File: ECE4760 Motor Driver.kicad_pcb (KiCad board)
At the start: 6 copper layers, 43.2 x 52.1 mm, 156 parts, among them J1 IO, J100 Alternative Motor, J2 Motor / Power, J4 UART, J5 Debug, Q1 EPC23104, Q2 EPC23104, Q3 EPC23104, Q4 EPC23104, SW1 BOOT, U1 STM32G473V_B-C-E_Hx, U2 ACS711xEXLT-15AB, U3 ACS711xEXLT-15AB, U4 ACS711xEXLT-15AB, U5 AP7361C-33FGE, U6 ACS711xEXLT-15AB, U7 TPSM365R6, X1 48MHz

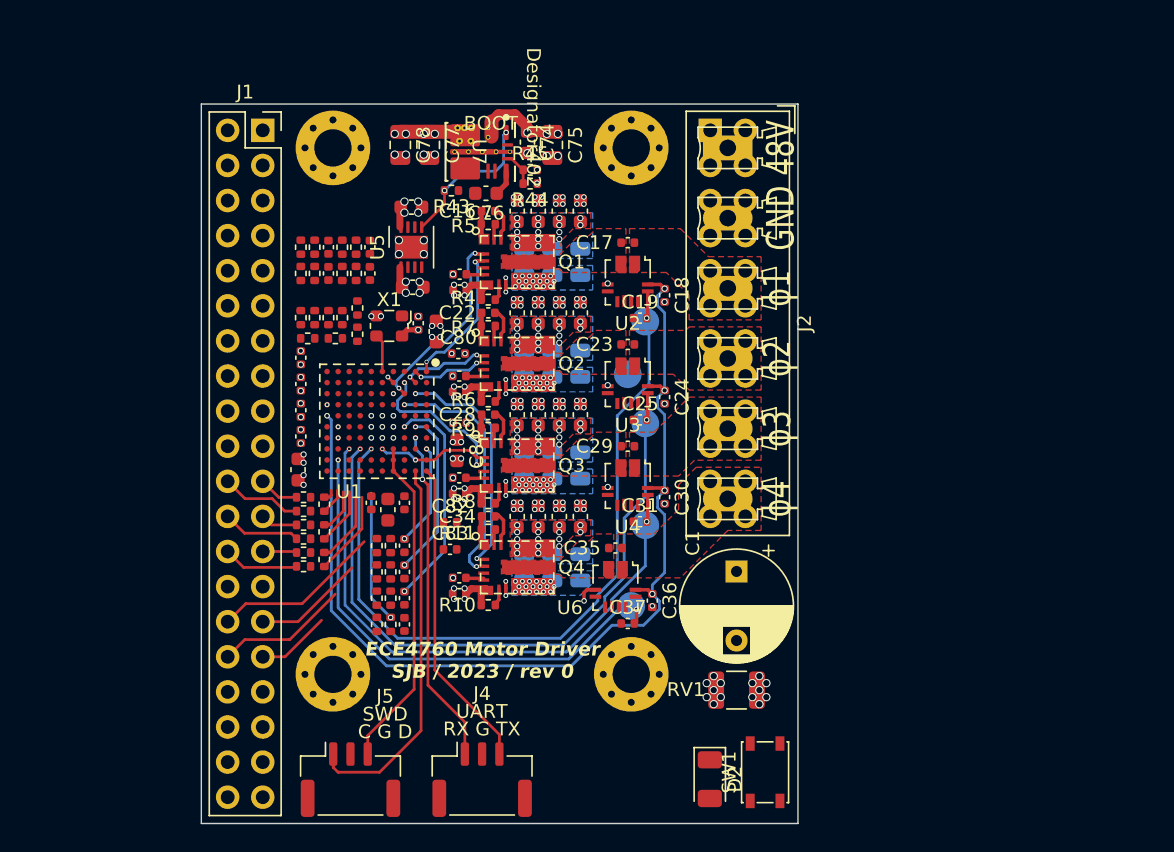
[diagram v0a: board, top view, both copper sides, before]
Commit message: Limit switch inputs and silkscreen
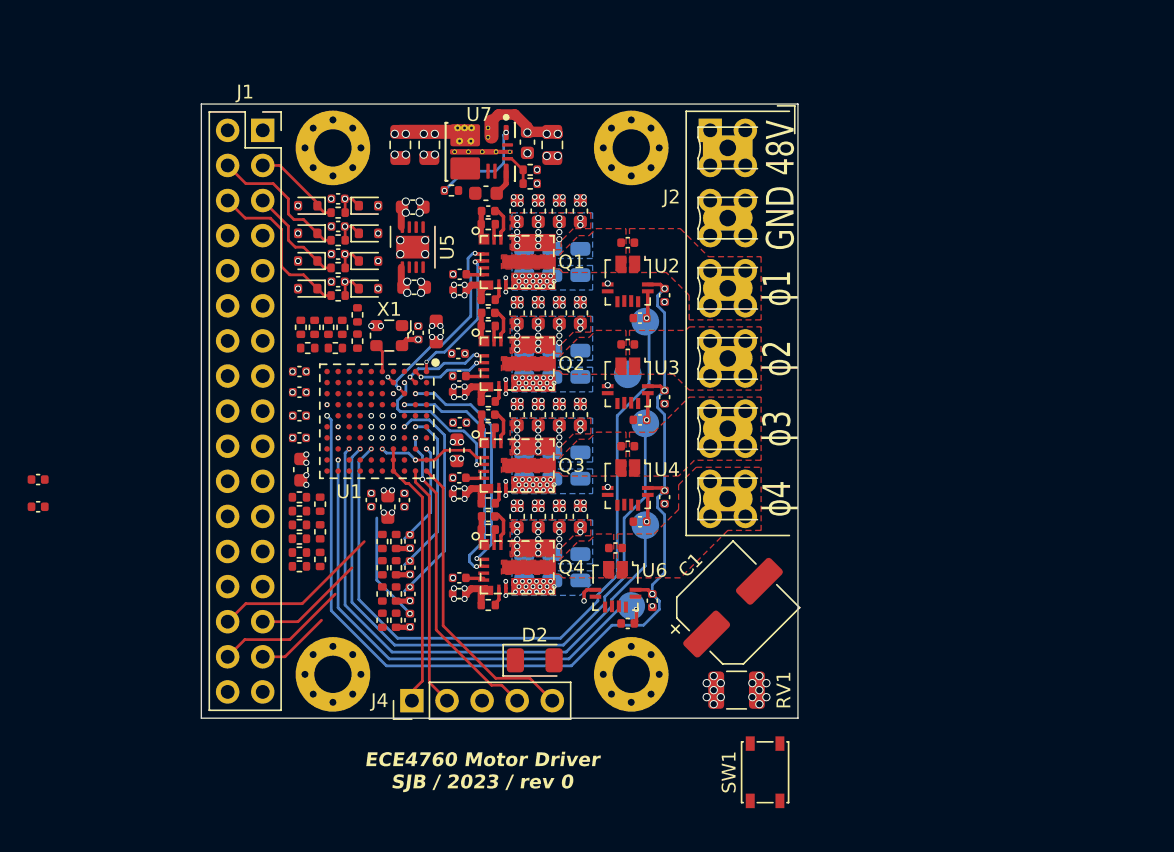
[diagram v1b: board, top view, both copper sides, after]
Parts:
- removed J5: Debug, Connector_JST:JST_GH_SM03B-GHS-TB_1x03-1MP_P1.25mm_Horizontal
- removed R36, R38, R40, R42: 1k, Resistor_SMD:R_0402_1005Metric
- added D1: D_Zener, Diode_SMD:D_SOD-523, F.Cu at (88.3, 50.0)
- added D3: D_Zener, Diode_SMD:D_SOD-523, F.Cu at (88.3, 48.0)
- added D4: D_Zener, Diode_SMD:D_SOD-523, F.Cu at (88.3, 54.0)
- added D5: D_Zener, Diode_SMD:D_SOD-523, F.Cu at (88.3, 52.0)
- added D6: D_Schottky, Diode_SMD:D_SOD-523, F.Cu at (83.9, 50.0)
- added D7: D_Schottky, Diode_SMD:D_SOD-523, F.Cu at (83.9, 48.0)
- added D8: D_Schottky, Diode_SMD:D_SOD-523, F.Cu at (83.9, 54.0)
- added D9: D_Schottky, Diode_SMD:D_SOD-523, F.Cu at (83.9, 52.0)
- C1: footprint Capacitor_THT:CP_Radial_D8.0mm_P5.00mm -> Capacitor_SMD:CP_Elec_6.3x7.7
- J1: footprint Connector_PinSocket_2.54mm:PinSocket_2x20_P2.54mm_Vertical -> Connector_PinSocket_2.54mm:PinSocket_2x17_P2.54mm_Vertical
- J4: footprint Connector_JST:JST_GH_SM03B-GHS-TB_1x03-1MP_P1.25mm_Horizontal -> Connector_PinHeader_2.54mm:PinHeader_1x05_P2.54mm_Vertical
- moved C82 30.0 mm to (64.4, 67.8)
- moved C83 30.0 mm to (64.4, 69.8)
- moved D2 15.3 mm to (100.3, 80.9), turned to 0 degrees
- moved J4 7.65 mm to (91.4, 83.8), turned to 90 degrees
- moved C71 5.45 mm to (86.1, 47.5), turned to 180 degrees
- moved R37 5.16 mm to (86.1, 48.5), turned to 0 degrees
- moved R39 3.51 mm to (86.1, 54.5), turned to 0 degrees
- moved C72 3.40 mm to (86.1, 53.5), turned to 180 degrees
- moved R35 2.75 mm to (86.1, 50.5), turned to 0 degrees
- moved C73 2.69 mm to (86.1, 51.5), turned to 180 degrees
- moved C1 2.63 mm to (114.7, 77.1), turned to 45 degrees
- moved C70 1.66 mm to (86.1, 49.5), turned to 180 degrees
- moved C9 1.00 mm to (83.3, 60.0), turned to 180 degrees
- moved C11 0.70 mm to (91.9, 57.2)
- moved R29 0.70 mm to (83.4, 56.8)
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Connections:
- J1 pad 3: Lim_H_In -> Lim_R_In
- J1 pad 6: Lim_R_In -> Lim_H_In
- J4 pad 1: /UART_RX -> /SWDIO
- J4 pad 2: GND -> /SWCLK
- J4 pad 3: /UART_TX -> GND
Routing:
- net Lim_H_In: track 0.00 -> 11.9 mm
- net Lim_L_In: track 0.00 -> 10.4 mm
- net /SWCLK: track 27.7 -> 17.6 mm
- net Lim_Aux_In: track 0.65 -> 7.56 mm
- net Lim_R_In: track 0.00 -> 6.48 mm
- net /ENC_I+: track 6.14 -> 0.00 mm
- net Enc_A_In+: track 5.88 -> 0.00 mm
- net Enc_B_In+: track 5.65 -> 0.00 mm
- net Enc_I_In+: track 5.49 -> 0.00 mm
- net /SWDIO: track 24.1 -> 18.6 mm
- net /ENC_I-: track 5.16 -> 0.00 mm
- net /ENC_B+: track 4.17 -> 0.00 mm
- net GND: track 6.20 -> 10.2 mm, vias 209 -> 229
- net Net-(U5-EN): track 10.7 -> 7.39 mm
- net /ENC_B-: track 3.19 -> 0.00 mm
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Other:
- board size 43.2 x 52.1 mm -> 43.2 x 44.5 mm
- board text added: "Clk"
- board text added: "Data"
- board text added: "Gnd"
- board text added: "Rx"
- board text added: "Tx"
- board text removed: "5V"
- board text removed: "C G D"
- board text removed: "RX G TX"
- board text removed: "SWD"
- board text removed: "UART"

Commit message: Update hall sensor circuit for 5V-tolerant pins
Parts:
- removed R13, R15, R17, R19: 1k, Resistor_SMD:R_0402_1005Metric
- removed SW1: BOOT, Button_Switch_SMD:SW_SPST_PTS810
- added R1: 1k, Resistor_SMD:R_0402_1005Metric, F.Cu at (83.3, 63.1)
- added R36: 1k, Resistor_SMD:R_0402_1005Metric, F.Cu at (83.3, 64.1)
- added R38: 330, Resistor_SMD:R_0402_1005Metric, F.Cu at (95.9, 78.4)
- added TP6: RESET, TestPoint:TestPoint_Pad_D2.0mm, B.Cu at (84.9, 57.5)
- added TP7: BOOT, TestPoint:TestPoint_Pad_D2.0mm, B.Cu at (95.2, 56.2)
- moved C69 3.16 mm to (90.7, 74.9), turned to 0 degrees
- moved R18 3.14 mm to (88.8, 74.9), turned to 0 degrees
- moved R29 3.10 mm to (86.5, 56.8)
- moved C66 2.28 mm to (90.7, 73.9), turned to 0 degrees
- moved R12 2.26 mm to (88.8, 73.9), turned to 0 degrees
- moved R31 2.10 mm to (86.0, 58.3), turned to 0 degrees
- moved R32 1.90 mm to (83.5, 56.8)
- moved R33 1.90 mm to (84.5, 56.8)
- moved R34 1.90 mm to (84.0, 58.3)
- moved R2 1.90 mm to (87.5, 57.8), turned to 90 degrees
- moved R3 1.90 mm to (87.5, 55.9), turned to 90 degrees
- moved C68 1.43 mm to (90.7, 72.9), turned to 0 degrees
- moved R16 1.39 mm to (88.8, 72.9), turned to 0 degrees
- moved C10 1.10 mm to (83.3, 62.1)
- moved R30 1.10 mm to (85.5, 56.8)
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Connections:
- C70 pad 1: /Limit Switch Input1/Out -> /LIM_L
- C71 pad 1: /Limit Switch Input2/Out -> /LIM_R
- C72 pad 1: /Limit Switch Input3/Out -> /LIM_H
- C73 pad 1: /Limit Switch Input4/Out -> /LIM_AUX
- D1 pad 1: /Limit Switch Input1/Out -> /LIM_L
- D2 pad 1: unconnected-(D2-K-Pad1) -> GND
- D2 pad 2: unconnected-(D2-A-Pad2) -> Net-(D2-A)
- D3 pad 1: /Limit Switch Input2/Out -> /LIM_R
- D4 pad 1: /Limit Switch Input3/Out -> /LIM_H
- D5 pad 1: /Limit Switch Input4/Out -> /LIM_AUX
- J1 pad 11: Aux_Enc_A_In+ -> Aux_Enc_A_In-
- J1 pad 12: Aux_Enc_A_In- -> Aux_Enc_A_In+
- J1 pad 15: ~{Fault_Enable} -> LED_1
- J1 pad 16: ~{Abort} -> LED_2
- J1 pad 17: LED_2 -> ~{Fault_Enable}
- J1 pad 18: LED_1 -> ~{Abort}
- R2 pad 2: Net-(U1-PA1) -> Net-(R2-Pad2)
- R29 pad 1: Aux_Enc_A_In+ -> Aux_Enc_B_In+
- R29 pad 2: /AUX_ENC_A+ -> /AUX_ENC_B+
- R3 pad 1: Net-(U1-PA1) -> Net-(R2-Pad2)
- R30 pad 1: Aux_Enc_A_In- -> Aux_Enc_B_In-
- R30 pad 2: /AUX_ENC_A- -> /AUX_ENC_B-
- R31 pad 1: /AUX_ENC_A- -> /AUX_ENC_B-
- R31 pad 2: /AUX_ENC_A+ -> /AUX_ENC_B+
- R32 pad 1: Aux_Enc_B_In+ -> Aux_Enc_A_In+
- R32 pad 2: /AUX_ENC_B+ -> /AUX_ENC_A+
- R33 pad 1: Aux_Enc_B_In- -> Aux_Enc_A_In-
- R33 pad 2: /AUX_ENC_B- -> /AUX_ENC_A-
- R34 pad 1: /AUX_ENC_B- -> /AUX_ENC_A-
- R34 pad 2: /AUX_ENC_B+ -> /AUX_ENC_A+
- R35 pad 2: /Limit Switch Input1/Out -> /LIM_L
- R37 pad 2: /Limit Switch Input2/Out -> /LIM_R
- R39 pad 2: /Limit Switch Input3/Out -> /LIM_H
- R41 pad 2: /Limit Switch Input4/Out -> /LIM_AUX
- U1 pad D1: unconnected-(U1-PC15-PadD1) -> /LIM_R
- U1 pad E10: unconnected-(U1-PA8-PadE10) -> Net-(U1-PA8)
- U1 pad E2: unconnected-(U1-PF1-PadE2) -> /LIM_L
- U1 pad F1: unconnected-(U1-PC2-PadF1) -> /LIM_H
- U1 pad F10: unconnected-(U1-PC7-PadF10) -> /HALL_I
- U1 pad F2: unconnected-(U1-PC0-PadF2) -> /LIM_AUX
- U1 pad G1: /HALL_I -> /AUX_ENC_B+
- U1 pad G2: Net-(U1-PA1) -> /AUX_ENC_B+
- U1 pad G6: /AUX_ENC_A+ -> unconnected-(U1-PE12-PadG6)
- U1 pad H1: /AUX_ENC_B -> /AUX_ENC_B-
- U1 pad H2: /AUX_ENC_A+ -> /AUX_ENC_B-
- U1 pad H3: unconnected-(U1-PA3-PadH3) -> Net-(R2-Pad2)
- U1 pad H4: /AUX_ENC_A+ -> unconnected-(U1-PB0-PadH4)
- U1 pad J1: /AUX_ENC_B- -> /AUX_ENC_A-
- U1 pad J2: /AUX_ENC_A- -> unconnected-(U1-PA6-PadJ2)
- U1 pad J4: /AUX_ENC_A- -> unconnected-(U1-PB2-PadJ4)
- U1 pad J6: ~{Abort} -> unconnected-(U1-PE11-PadJ6)
- U1 pad J7: LED_2 -> unconnected-(U1-PE14-PadJ7)
- U1 pad K1: /AUX_ENC_B+ -> /AUX_ENC_A+
- U1 pad K10: LED_1 -> unconnected-(U1-PD8-PadK10)
- U1 pad K2: unconnected-(U1-PC4-PadK2) -> LED_1
- U1 pad K3: unconnected-(U1-PB1-PadK3) -> LED_2
- U1 pad K6: ~{Fault_Enable} -> Net-(U1-PE10)
- U1 pad K7: /AUX_ENC_B -> Net-(U1-PE13)
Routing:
- net /LIM_R: track 0.00 -> 17.1 mm, vias 0 -> 2
- net /LIM_L: track 0.00 -> 15.8 mm, vias 0 -> 2
- net Net-(U1-PA8): track 0.00 -> 15.0 mm, vias 0 -> 2
- net /LIM_AUX: track 0.00 -> 13.7 mm, vias 0 -> 2
- net /LIM_H: track 0.00 -> 10.7 mm, vias 0 -> 2
- net Aux_Enc_B_In-: track 0.00 -> 9.09 mm
- net /~{RST}: track 0.00 -> 8.75 mm, vias 0 -> 1
- net LED_2: track 0.00 -> 7.72 mm
- net Aux_Enc_B_In+: track 0.00 -> 7.34 mm
- net /BOOT_SELECT: track 0.00 -> 6.52 mm, vias 0 -> 1
- net Aux_Enc_A_In+: track 0.11 -> 5.92 mm
- net Net-(R2-Pad2): track 0.00 -> 5.44 mm, vias 0 -> 2
- net ~{Abort}: track 0.00 -> 5.19 mm, vias 1 -> 0
- net LED_1: track 0.00 -> 4.85 mm, vias 0 -> 1
- net Hall_I_In: track 5.35 -> 10.0 mm
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
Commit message: Ready for design review
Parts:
- removed the D5 at (88.3, 52.0)
- removed D6, D7, D8, D9: D_Schottky, Diode_SMD:D_SOD-523
- removed the R1 at (83.3, 63.1)
- removed the R36 at (83.3, 64.1)
- removed the R43 at (94.3, 46.9)
- added C81: 100n, Capacitor_SMD:C_0402_1005Metric, B.Cu at (88.8, 64.9)
- added C82: 100n, Capacitor_SMD:C_0402_1005Metric, B.Cu at (90.2, 64.5)
- added D2: BAT54XY, Package_TO_SOT_SMD:SOT-363_SC-70-6, F.Cu at (88.6, 73.2)
- added R12: 4k7, Resistor_SMD:R_0402_1005Metric, F.Cu at (90.5, 76.1)
- added R14: 4k7, Resistor_SMD:R_0402_1005Metric, F.Cu at (90.5, 78.0)
- added R16: 4k7, Resistor_SMD:R_0402_1005Metric, F.Cu at (90.5, 72.3)
- added R18: 4k7, Resistor_SMD:R_0402_1005Metric, F.Cu at (90.5, 74.2)
- added R20: 4k7, Resistor_SMD:R_0402_1005Metric, F.Cu at (87.6, 49.7)
- added R22: 4k7, Resistor_SMD:R_0402_1005Metric, F.Cu at (87.6, 47.8)
- added R24: 4k7, Resistor_SMD:R_0402_1005Metric, F.Cu at (87.6, 53.5)
- added R26: 4k7, Resistor_SMD:R_0402_1005Metric, F.Cu at (87.6, 51.6)
- C1: value 10u 100V -> 22u 100V
- C18: renamed from C16; value 100n, 6V -> 100n
- C20: renamed from C18; value 10n -> 1n
- C31: renamed from C22; value 100n, 6V -> 100n
- C33: renamed from C24; value 10n -> 1n
- C44: renamed from C28; value 100n, 6V -> 100n
- C46: renamed from C30; value 10n -> 1n
- C57: renamed from C34; value 100n, 6V -> 100n
- C59: renamed from C36; value 10n -> 1n
- C61: renamed from C66; value 10n -> 1n
- C62: renamed from C67; value 10n -> 1n
- C63: renamed from C68; value 10n -> 1n
- C64: renamed from C69; value 10n -> 1n
- C7: renamed from C76; value 1u -> 4u7
- C70: renamed from C5; value 1u -> 4u7
- C71: renamed from C4; value 1u -> 4u7
- C72: renamed from C85; value 1u -> 4u7
- C73: renamed from C84; value 1u -> 4u7
- C83: renamed from C82; moved to B.Cu
- C84: renamed from C83; moved to B.Cu
- D1, D3, D4: value D_Zener -> BAT54XY; footprint Diode_SMD:D_SOD-523 -> Package_TO_SOT_SMD:SOT-363_SC-70-6
- D5: renamed from D2; value LED -> Green
- R13: renamed from R12; value 1k -> 100
- R15: renamed from R14; value 1k -> 100
- R17: renamed from R16; value 1k -> 100
- R19: renamed from R18; value 1k -> 100
- R21: renamed from R35; value 1k -> 100
- R23: renamed from R37; value 1k -> 100
- R25: renamed from R39; value 1k -> 100
- R27: renamed from R41; value 1k -> 100
- R31: renamed from R20; value 1k, 0.1% -> 1k, 1%
- R32: renamed from R22; value 1k, 0.1% -> 1k, 1%
- R33: renamed from R21; value 1k, 0.1% -> 1k, 1%
- R34: renamed from R23; value 1k, 0.1% -> 1k, 1%
- R35: renamed from R25; value 1k, 0.1% -> 1k, 1%
- R36: renamed from R24; value 1k, 0.1% -> 1k, 1%
- R37: renamed from R26; value 1k, 0.1% -> 1k, 1%
- R38: renamed from R28; value 1k, 0.1% -> 1k, 1%
- R39: renamed from R27; value 1k, 0.1% -> 1k, 1%
- R40: renamed from R29; value 1k, 0.1% -> 1k, 1%
- R41: renamed from R31; value 1k, 0.1% -> 1k, 1%
- R42: renamed from R30; value 1k, 0.1% -> 1k, 1%
- R43: renamed from R32; value 1k, 0.1% -> 1k, 1%
- R44: renamed from R34; value 1k, 0.1% -> 1k, 1%
- R45: renamed from R33; value 1k, 0.1% -> 1k, 1%
- TP3: renamed from TP1; value TestPoint -> Sense
- TP4: renamed from TP2; value TestPoint -> Sense
- TP5: renamed from TP3; value TestPoint -> Sense
- TP6: renamed from TP4; value TestPoint -> Sense
- TP7: renamed from TP5; value TestPoint -> Sense
- moved D1 27.0 mm to (88.6, 77.0), turned to 90 degrees
- moved C83 25.8 mm to (89.8, 63.1), turned to 180 degrees
- moved C84 24.8 mm to (88.4, 63.5), turned to -90 degrees
- moved R15 6.63 mm to (86.2, 78.0)
- moved C62 6.15 mm to (91.5, 78.0), turned to 90 degrees
- moved R13 3.97 mm to (86.2, 76.9)
- moved R17 3.16 mm to (86.2, 74.7)
- moved D4 3.00 mm to (85.7, 52.5), turned to -90 degrees
- moved R19 2.75 mm to (86.2, 75.8)
- moved D3 2.67 mm to (85.7, 48.6), turned to -90 degrees
- moved C66 2.52 mm to (88.6, 47.8), turned to -90 degrees
- moved C65 2.51 mm to (88.6, 49.7), turned to 90 degrees
- moved R25 2.51 mm to (83.8, 53.5), turned to 90 degrees
- moved C68 2.50 mm to (88.6, 51.6), turned to -90 degrees
- moved C67 2.50 mm to (88.6, 53.5), turned to 90 degrees
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- renumbered C39 to C10, C40 to C11, C41 to C12, C54 to C13, C55 to C14, C56 to C15, C14 to C16, C15 to C17, C17 to C19, C74 to C2, C19 to C21, C42 to C22, C43 to C23, C44 to C24, C45 to C25, C57 to C26, C58 to C27, C59 to C28, C20 to C29, C75 to C3, C21 to C30, C23 to C32, C25 to C34, C46 to C35, C47 to C36, C48 to C37, C49 to C38, C60 to C39, C78 to C4, C61 to C40, C62 to C41, C26 to C42, C27 to C43, C29 to C45, C31 to C47, C50 to C48, C51 to C49, C77 to C5, C52 to C50, C53 to C51, C63 to C52, C64 to C53, C65 to C54, C32 to C55, C33 to C56, C35 to C58, C12 to C6, C37 to C60, C70 to C65, C71 to C66, C72 to C67, C73 to C68, C10 to C69, C79 to C74, C80 to C75, C81 to C76, C9 to C77, C8 to C78, C7 to C79, C13 to C8, C6 to C80, C11 to C85, C38 to C9, J100 to J101, J4 to J3, R44 to R1, R2 to R28, R3 to R29, R45 to R3, R38 to R30, TP6 to TP1, TP7 to TP2, U6 to U5, U5 to U6
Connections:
- C20 pad 2: VREF -> +3V3
- C33 pad 2: VREF -> +3V3
- C46 pad 2: VREF -> +3V3
- C59 pad 2: VREF -> +3V3
- C62 pad 1: /HALL_B -> /HALL_I
- C63 pad 1: /HALL_C -> /HALL_B
- C64 pad 1: /HALL_I -> /HALL_C
- D1 pad 1: /LIM_L -> GND
- D1 pad 2: GND -> +5V
- D3 pad 1: /LIM_R -> GND
- D3 pad 2: GND -> +5V
- D4 pad 1: /LIM_H -> GND
- D4 pad 2: GND -> +5V
- R15 pad 1: Hall_B_In -> Hall_I_In
- R15 pad 2: /HALL_B -> /HALL_I
- R17 pad 1: Hall_C_In -> Hall_B_In
- R17 pad 2: /HALL_C -> /HALL_B
- R19 pad 1: Hall_I_In -> Hall_C_In
- R19 pad 2: /HALL_I -> /HALL_C
- U1 pad B4: unconnected-(U1-PB7-PadB4) -> /PH4_LO
- U1 pad F10: /HALL_I -> /ENC_I+
- U1 pad F9: unconnected-(U1-PC6-PadF9) -> /HALL_I
- U1 pad G6: unconnected-(U1-PE12-PadG6) -> /AUX_ENC_A-
- U1 pad G9: unconnected-(U1-PD13-PadG9) -> /ENC_I+
- U1 pad J2: unconnected-(U1-PA6-PadJ2) -> Net-(U1-PA6)
- U1 pad J6: unconnected-(U1-PE11-PadJ6) -> ~{Abort}
- U1 pad K5: VREF -> +3V3
- U1 pad K6: Net-(U1-PE10) -> ~{Fault_Enable}
- U1 pad K7: Net-(U1-PE13) -> Net-(U1-PA6)
- U2 pad 10: VREF -> +3V3
- U3 pad 10: VREF -> +3V3
- U4 pad 10: VREF -> +3V3
- U5 pad 10: VREF -> +3V3
- U6 pad 5: Net-(U5-EN) -> +5V
- U7 pad 1: Net-(U5-EN) -> unconnected-(U7-PGOOD-Pad1)
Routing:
- net +3V3: track 6.81 -> 83.9 mm, vias 25 -> 30
- net VREF: track 71.7 -> 0.00 mm, vias 5 -> 0
- net GND: track 5.64 -> 18.3 mm, vias 242 -> 250
- net /ENC_I+: track 0.00 -> 11.4 mm
- net Net-(U5-EN): track 10.7 -> 0.00 mm, vias 2 -> 0
- net /HALL_I: track 11.5 -> 19.9 mm, vias 1 -> 2
- net /ENC_I-: track 0.00 -> 8.31 mm
- net /HALL_B: track 6.95 -> 14.1 mm, vias 1 -> 2
- net /ENC_B-: track 0.00 -> 7.00 mm
- net /ENC_B+: track 0.00 -> 6.89 mm
- net /HALL_C: track 11.6 -> 18.3 mm, vias 1 -> 2
- net /HALL_A: track 15.6 -> 21.6 mm, vias 1 -> 2
- net Enc_A_In+: track 0.00 -> 5.58 mm
- net Enc_I_In+: track 0.00 -> 5.38 mm
- net Enc_B_In+: track 0.00 -> 5.35 mm
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- removed copper zone on In1.Cu, net Aux_Enc_A_In-
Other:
- board text added: "SWC"
- board text added: "SWD"
- board text removed: "BOOT"
- board text removed: "ECE4760 Motor Driver SJB / 2023 rev 0"

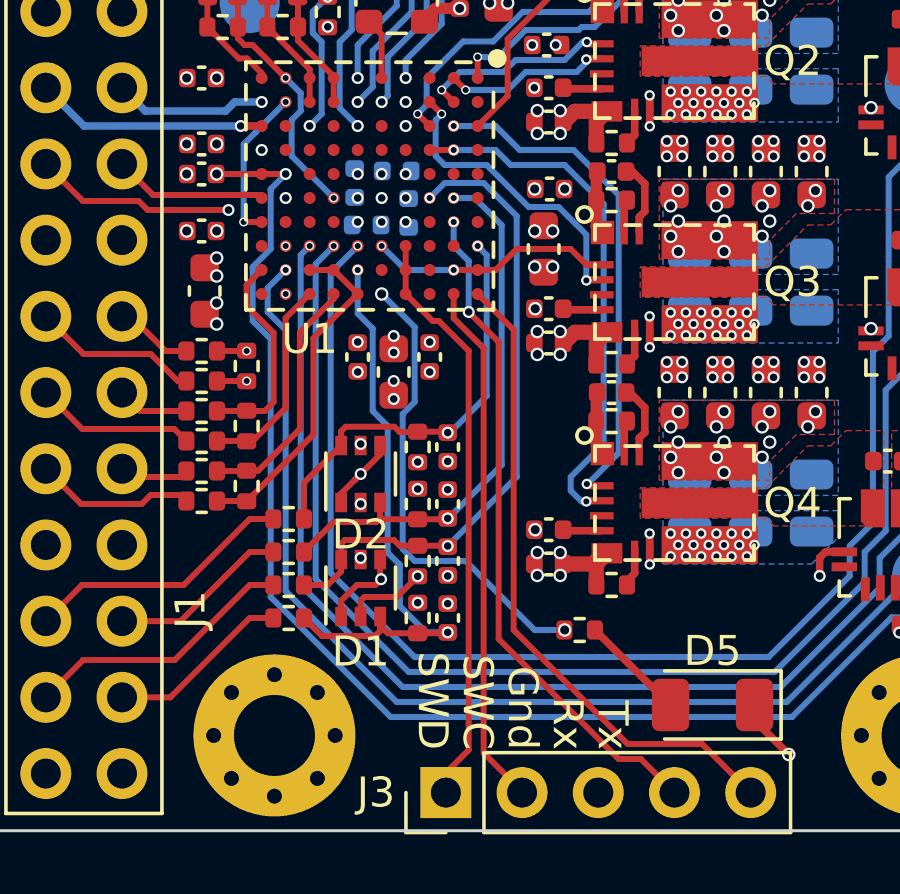
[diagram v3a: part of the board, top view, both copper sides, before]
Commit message: Tweaking pin assignments
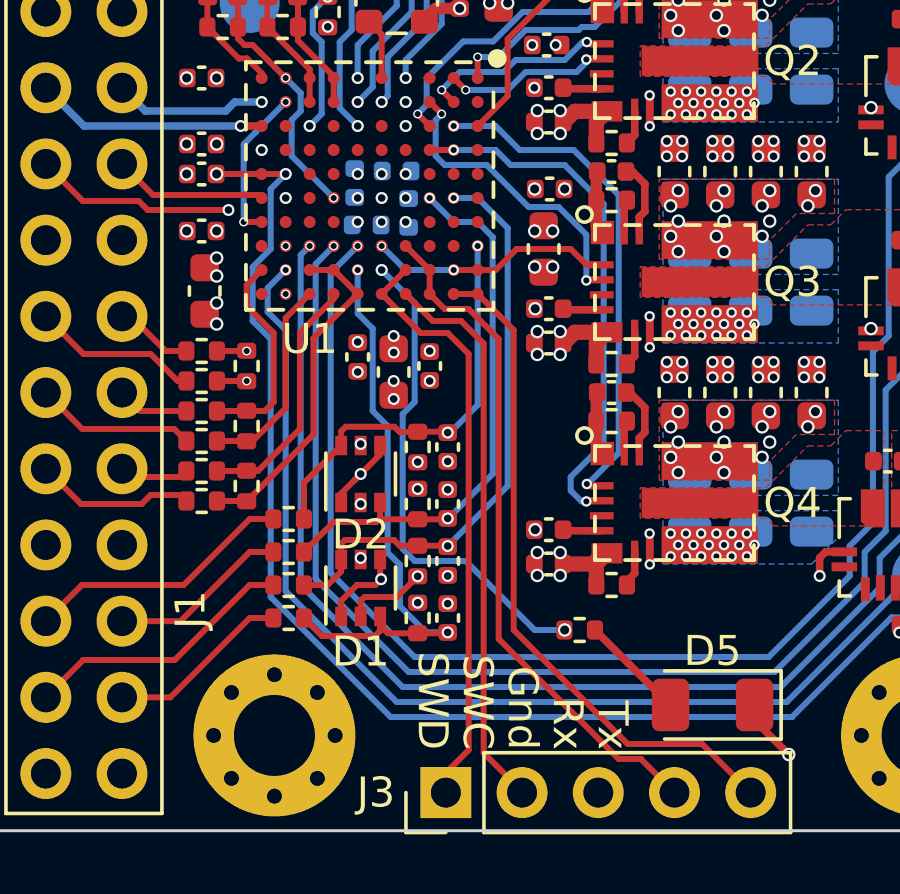
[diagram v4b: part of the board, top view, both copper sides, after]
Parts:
- C20, C33, C46, C59: value 1n -> 100n
- C21, C34, C47, C60: value 100n -> 1n
- moved C74 0.30 mm to (90.9, 69.6)
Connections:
- C61 pad 1: /HALL_A -> /HALL_C
- C64 pad 1: /HALL_C -> /HALL_A
- D1 pad 6: /HALL_A -> /HALL_C
- D2 pad 3: /HALL_C -> /HALL_A
- J1 pad 29: Hall_C_In -> Hall_A_In
- J1 pad 32: Hall_A_In -> Hall_C_In
- J3 pad 1: /SWDIO -> /UART_RX
- J3 pad 2: /SWCLK -> /UART_TX
- J3 pad 4: /UART_RX -> /SWDIO
- J3 pad 5: /UART_TX -> /SWCLK
- R12 pad 2: /HALL_A -> /HALL_C
- R13 pad 1: Hall_A_In -> Hall_C_In
- R13 pad 2: /HALL_A -> /HALL_C
- R18 pad 2: /HALL_C -> /HALL_A
- R19 pad 1: Hall_C_In -> Hall_A_In
- R19 pad 2: /HALL_C -> /HALL_A
- R30 pad 2: Net-(U1-PA8) -> Net-(U1-PC9)
- U1 pad A10: /UART_TX -> /SWCLK
- U1 pad B7: /UART_RX -> unconnected-(U1-PD2-PadB7)
- U1 pad C10: unconnected-(U1-PA11-PadC10) -> /SWDIO
- U1 pad C9: unconnected-(U1-PA12-PadC9) -> /SWDIO
- U1 pad D10: /SWDIO -> /UART_TX
- U1 pad D9: /SWDIO -> /UART_RX
- U1 pad E10: Net-(U1-PA8) -> /UART_RX
- U1 pad E9: unconnected-(U1-PC9-PadE9) -> Net-(U1-PC9)
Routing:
- net Net-(U1-PC9): track 0.00 -> 16.4 mm, vias 0 -> 2
- net Net-(U1-PA8): track 15.6 -> 0.00 mm, vias 2 -> 0
- net /SWCLK: track 17.6 -> 22.6 mm
- net /SWDIO: track 18.6 -> 22.8 mm
- net /UART_RX: track 22.5 -> 18.9 mm, vias 2 -> 0
- net Hall_C_In: track 6.00 -> 9.14 mm
- net Hall_A_In: track 9.14 -> 6.00 mm
- net /HALL_A: track 21.6 -> 18.5 mm
- net /UART_TX: track 21.8 -> 18.8 mm
- net /HALL_C: track 18.3 -> 19.7 mm
